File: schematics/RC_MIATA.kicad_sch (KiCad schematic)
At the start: 3 parts, among them U1 ESP32-C3-DevKitM-1, U2 LM7805_TO220

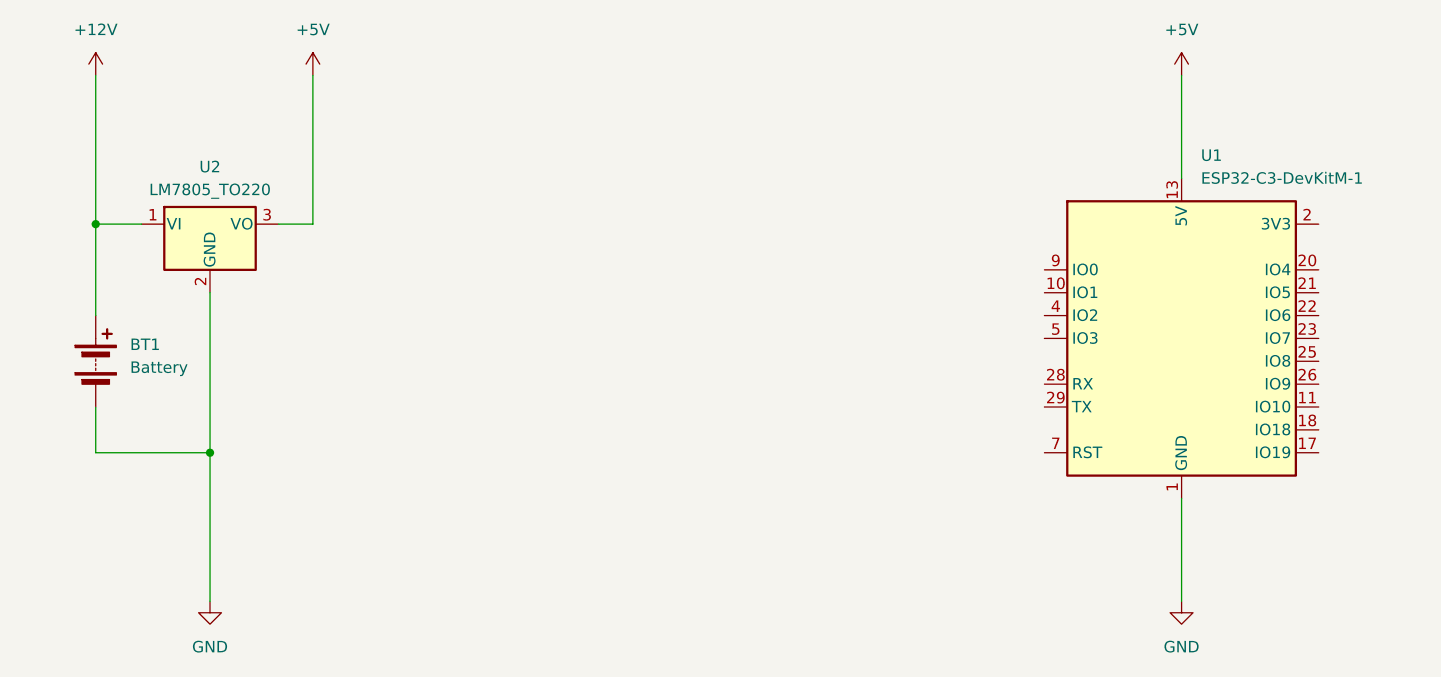
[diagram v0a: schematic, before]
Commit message: Created ESC and BDLC Symbols. Added to schematic unwired
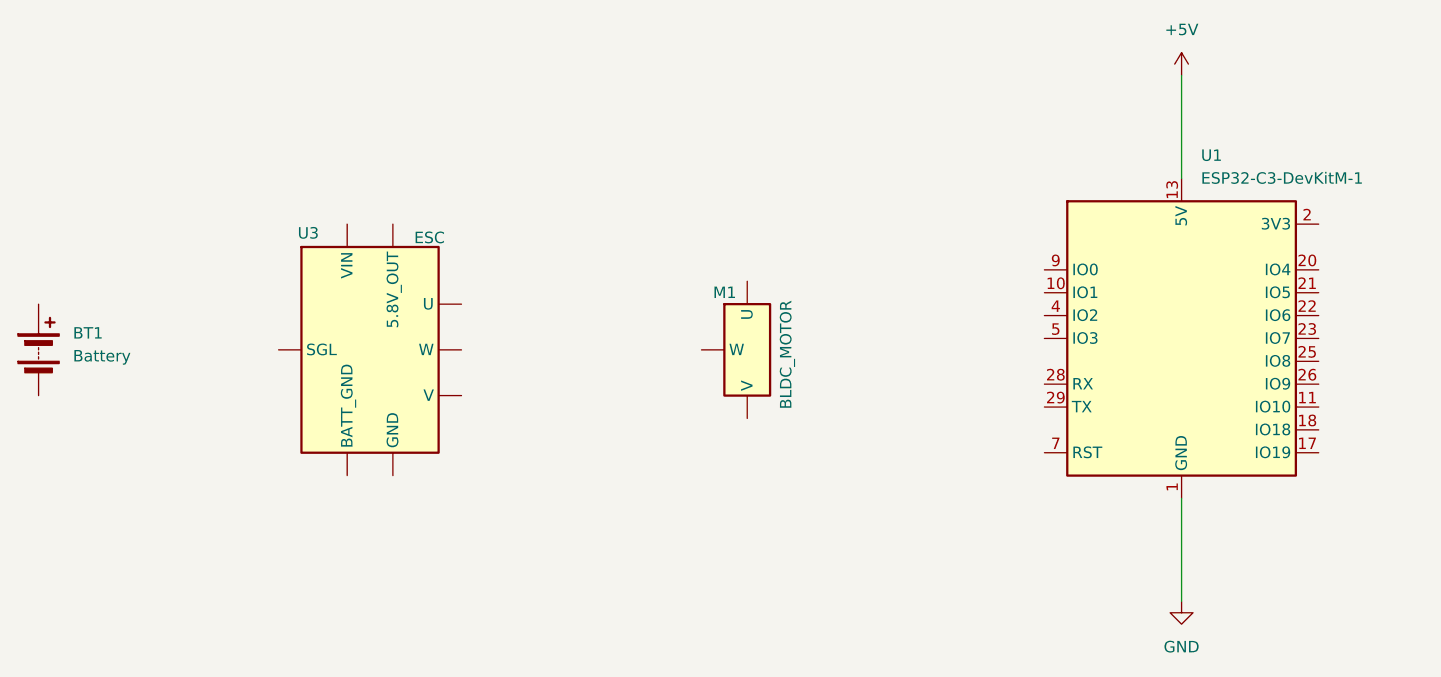
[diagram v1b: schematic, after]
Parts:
- removed U2: LM7805_TO220, Package_TO_SOT_THT:TO-220-3_Vertical, symbol Regulator_Linear:LM7805_TO220
- added M1: BLDC_MOTOR, symbol RC Components:BLDC_MOTOR
- added U3: ESC, symbol RC Components:60A_BRUSHLESS_ESC
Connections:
- net GND: no longer BT1.2 (-)
- net +12V: no longer names the net of BT1.1 (+)
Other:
- moved on the sheet: BT1
